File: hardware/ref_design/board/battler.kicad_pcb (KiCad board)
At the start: 2 copper layers, 73.4 x 127.7 mm, 177 parts, among them J1 TYPE-C-31-M-12, J2 53261-0271, J3 FH12-50S-0.5SH(55), J4 53261-0271, J5 SWD, J6 UART, J7 DEBUG PADS, Q1 2N7002, Q3 2N7002, Q5 AO3400A, Q6 AO3400A, Q7 2N7002, SW1 P1 UP, SW10 P2 DOWN, SW11 P2 LEFT, SW12 P2 RIGHT, SW13 P2 A, SW14 P2 B, SW15 P2 X, SW16 P2 Y, SW18 BOOTSEL, SW19 RESET, SW2 P1 DOWN, SW20 P1 SELECT, SW21 P1 START / PWR, SW22 P2 SELECT, SW23 P2 START / PWR, SW3 P1 LEFT, SW4 P1 RIGHT, SW5 P1 A, SW6 P1 B, SW7 P1 X, SW8 P1 Y, SW9 P2 UP, U1 SRV05-4, U2 BQ24073RGTR, U3 RT9013-33GB, U4 RP2354B, U6 MCP6002, U7 FM8002A, U8 SN74HC165PWR, U9 SN74HC165PWR, X1 12MHz

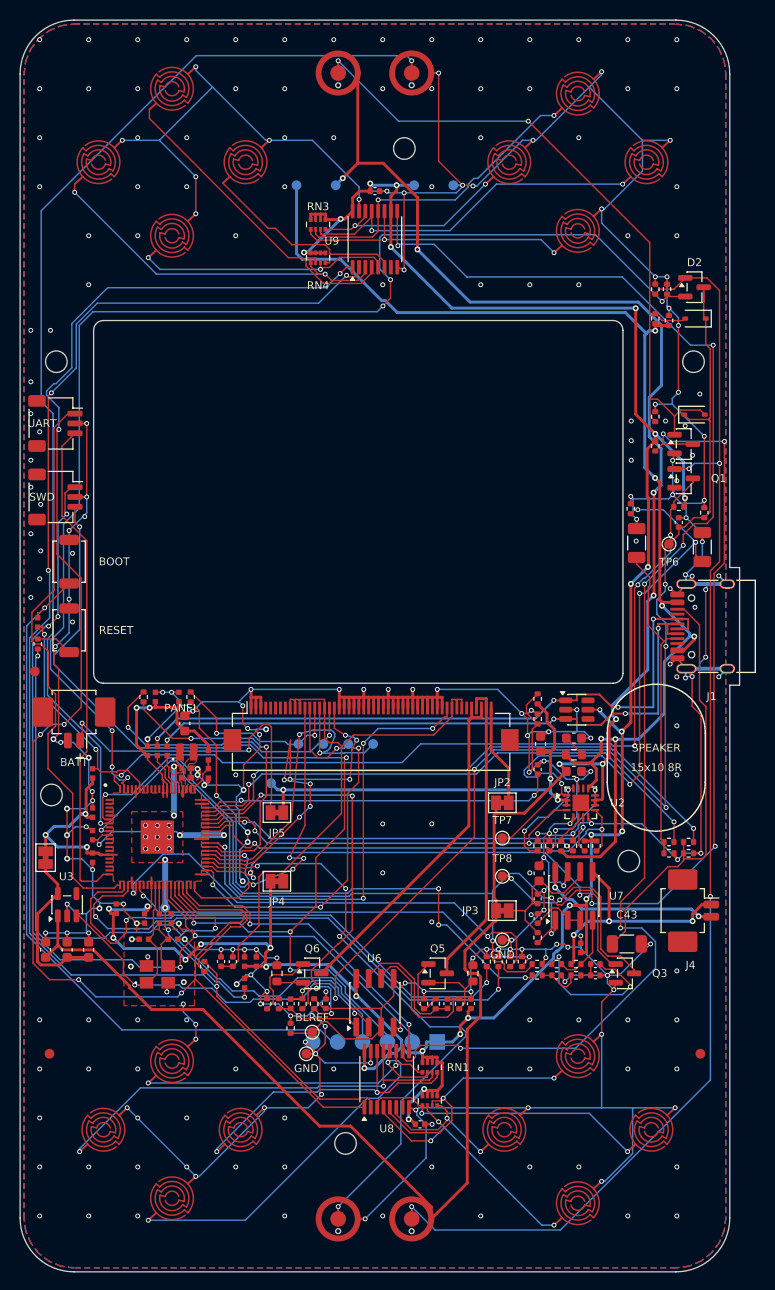
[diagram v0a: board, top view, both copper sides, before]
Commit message: ref_design levers: pins facing their nets, no REV straps, no UART, debug buttons and latch parts out of the strips
An experiment for Alex (not on ref-design-cellcut): make the board easier to route without
changing its size.
1. GPIOs: AUDIO_PWM 8 -> 31 (PWM7 B), AMP_EN 11 -> 34, BL_PWM 44 -> 28 (PWM6 A), PWR_HOLD
   2 -> 44, P2_START 34 -> 2, P2_SELECT 9 -> 4, SR_PL 28 -> 19 (datasheet Table 3 checked;
   U4's pin review updated)
2. REV0-REV3 and R48-R51 removed (the revision stays on the silkscreen)
3. J6 (UART) and C41 removed; SW18/SW19 out of the left strip into the left bezel below H4
   (U3 and its caps 2 mm down, JP1 below the core)
4. The latch's strip parts (Q1, R16, R15, C47, TP6, D8, Q7, R62, R63) up past the hole's
   top edge under seat 2's deck; C42 to the right bezel
tools/strip_load.py counts nets through each strip: 11/15 -> 8/11, parts 8/16 -> 3/5.
Routed clean on the first finished attempt (seed 3, 4.2 min); check_pcb and check_fit pass.

Co-Authored-By: Claude Opus 5.5 <noreply@anthropic.com>
Claude-Session: https://claude.ai/code/session_01Y3mFMxLYqNeyyedvbYuRwX
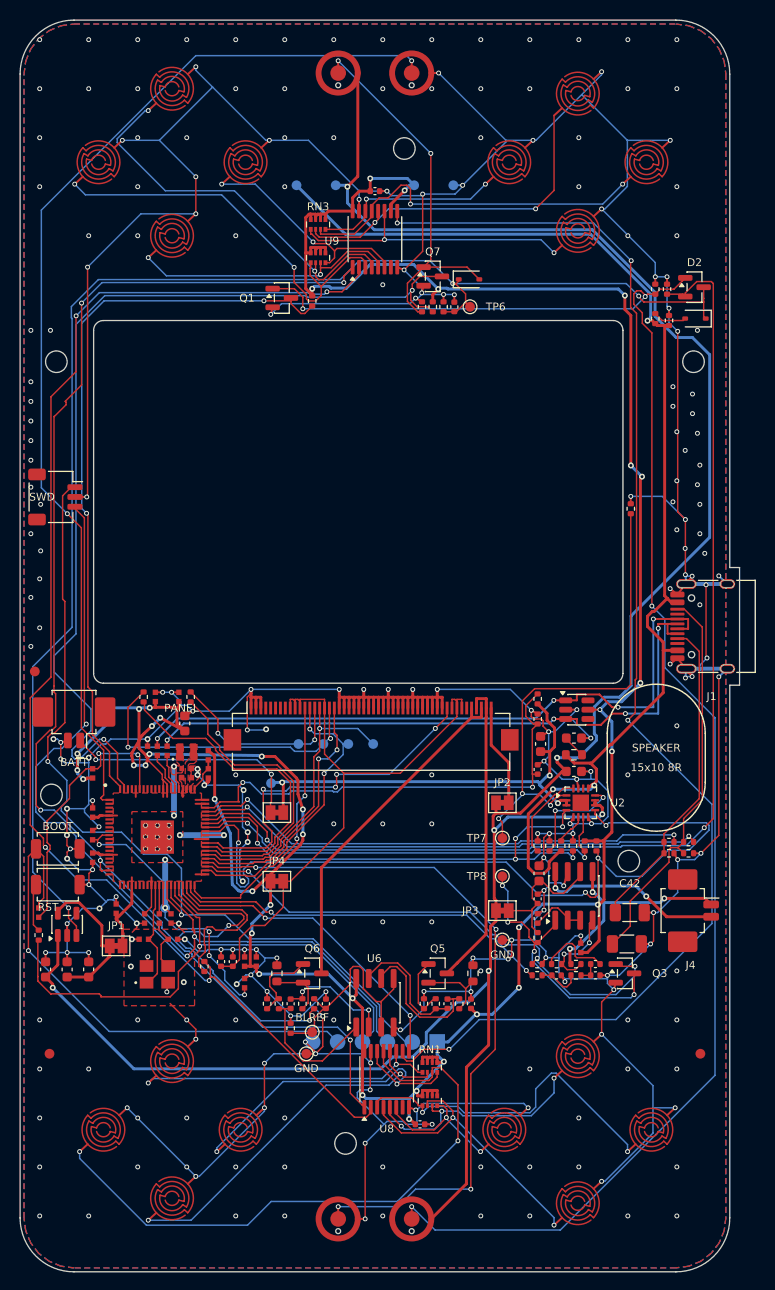
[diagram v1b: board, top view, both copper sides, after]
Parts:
- removed C41: DNP, Capacitor_SMD:C_1206_3216Metric
- removed J6: UART, battler:JST_SH_SM03B-SRSS-TB_1x03-1MP_P1.00mm_Horizontal
- removed R48: DNP, Resistor_SMD:R_0402_1005Metric
- removed R49, R50, R51: 1k, Resistor_SMD:R_0402_1005Metric
- moved Q1 44.9 mm to (90.5, 64.5)
- moved R16 42.9 mm to (93.6, 64.8), turned to 90 degrees
- moved C42 37.7 mm to (126.0, 127.2), turned to 0 degrees
- moved R15 33.9 mm to (107.0, 65.4)
- moved C47 31.8 mm to (108.1, 65.4)
- moved TP6 31.6 mm to (109.7, 65.4)
- moved Q7 30.8 mm to (105.9, 62.3)
- moved R26 29.7 mm to (65.7, 129.5)
- moved R25 29.6 mm to (65.7, 127.2)
- moved SW18 29.3 mm to (67.7, 120.7), turned to 0 degrees
- moved D8 26.8 mm to (109.6, 62.6)
- moved R63 26.8 mm to (105.9, 65.4)
- moved R62 26.3 mm to (104.8, 65.4)
- moved SW19 26.0 mm to (67.7, 124.3), turned to 0 degrees
- moved JP1 11.5 mm to (73.6, 130.6), turned to 0 degrees
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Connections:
- U4 pad 1: unconnected-(U4-GPIO4-Pad1) -> P2_SELECT
- U4 pad 19: unconnected-(U4-GPIO19-Pad19) -> SR_PL
- U4 pad 20: UART_TX -> unconnected-(U4-GPIO20-Pad20)
- U4 pad 21: UART_RX -> unconnected-(U4-GPIO21-Pad21)
- U4 pad 22: /MCU/REV0 -> unconnected-(U4-GPIO22-Pad22)
- U4 pad 23: /MCU/REV1 -> unconnected-(U4-GPIO23-Pad23)
- U4 pad 25: /MCU/REV2 -> unconnected-(U4-GPIO24-Pad25)
- U4 pad 26: /MCU/REV3 -> unconnected-(U4-GPIO25-Pad26)
- U4 pad 36: SR_PL -> BL_PWM
- U4 pad 39: unconnected-(U4-GPIO31-Pad39) -> AUDIO_PWM
- U4 pad 43: P2_START -> AMP_EN
- U4 pad 55: BL_PWM -> PWR_HOLD
- U4 pad 6: AUDIO_PWM -> unconnected-(U4-GPIO8-Pad6)
- U4 pad 7: P2_SELECT -> unconnected-(U4-GPIO9-Pad7)
- U4 pad 79: PWR_HOLD -> P2_START
- U4 pad 9: AMP_EN -> unconnected-(U4-GPIO11-Pad9)
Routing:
- net UART_RX: track 57.7 -> 0.00 mm
- net /MCU/REV0: track 55.6 -> 0.00 mm, vias 2 -> 0
- net /MCU/REV1: track 54.2 -> 0.00 mm, vias 2 -> 0
- net UART_TX: track 50.8 -> 0.00 mm
- net /MCU/REV2: track 49.8 -> 0.00 mm, vias 2 -> 0
- net /MCU/REV3: track 44.9 -> 0.00 mm, vias 2 -> 0
- net +3V3: track 309.3 -> 346.8 mm, vias 35 -> 37
- net PWR_BTN_RAW: track 132.6 -> 169.9 mm
- net CHG_STAT_N: track 48.5 -> 82.6 mm, vias 2 -> 4
- net AMP_EN: track 87.5 -> 55.0 mm
- net P2_START_RAW: track 67.9 -> 38.8 mm
- net RUN: track 83.2 -> 56.8 mm, vias 2 -> 1
- net SR_PL: track 160.9 -> 135.3 mm, vias 6 -> 5
- net AUDIO_PWM: track 64.4 -> 39.1 mm, vias 4 -> 2
- net /Debug/BOOTSEL: track 75.3 -> 52.7 mm
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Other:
- board text added: "RST"
- board text removed: "RESET"
- board text removed: "UART"

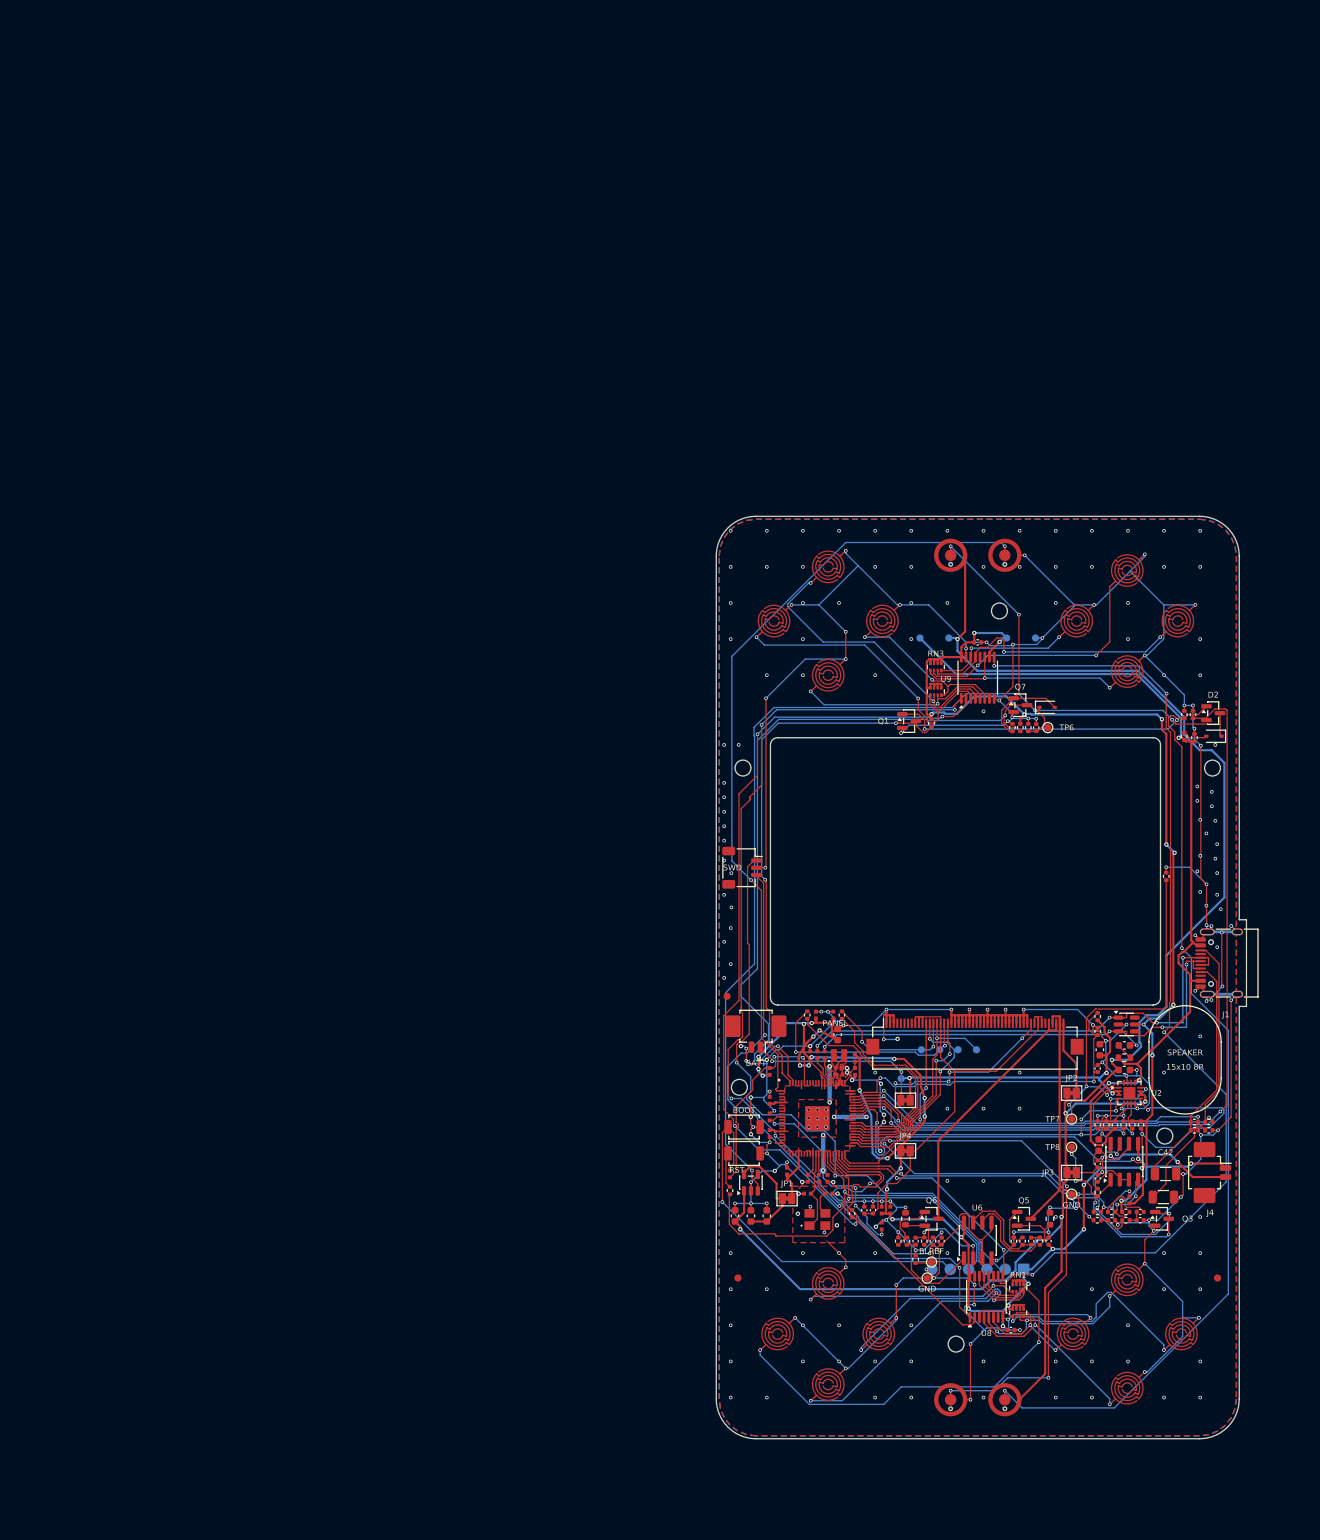
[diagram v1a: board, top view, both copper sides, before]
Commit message: ref_design: board routed for the 3.5 in panel (0 unconnected, DRC 0 errors); route.py's maze reaches across the board for SR_CHAIN
Co-Authored-By: Claude Sonnet 5.5 <noreply@anthropic.com>
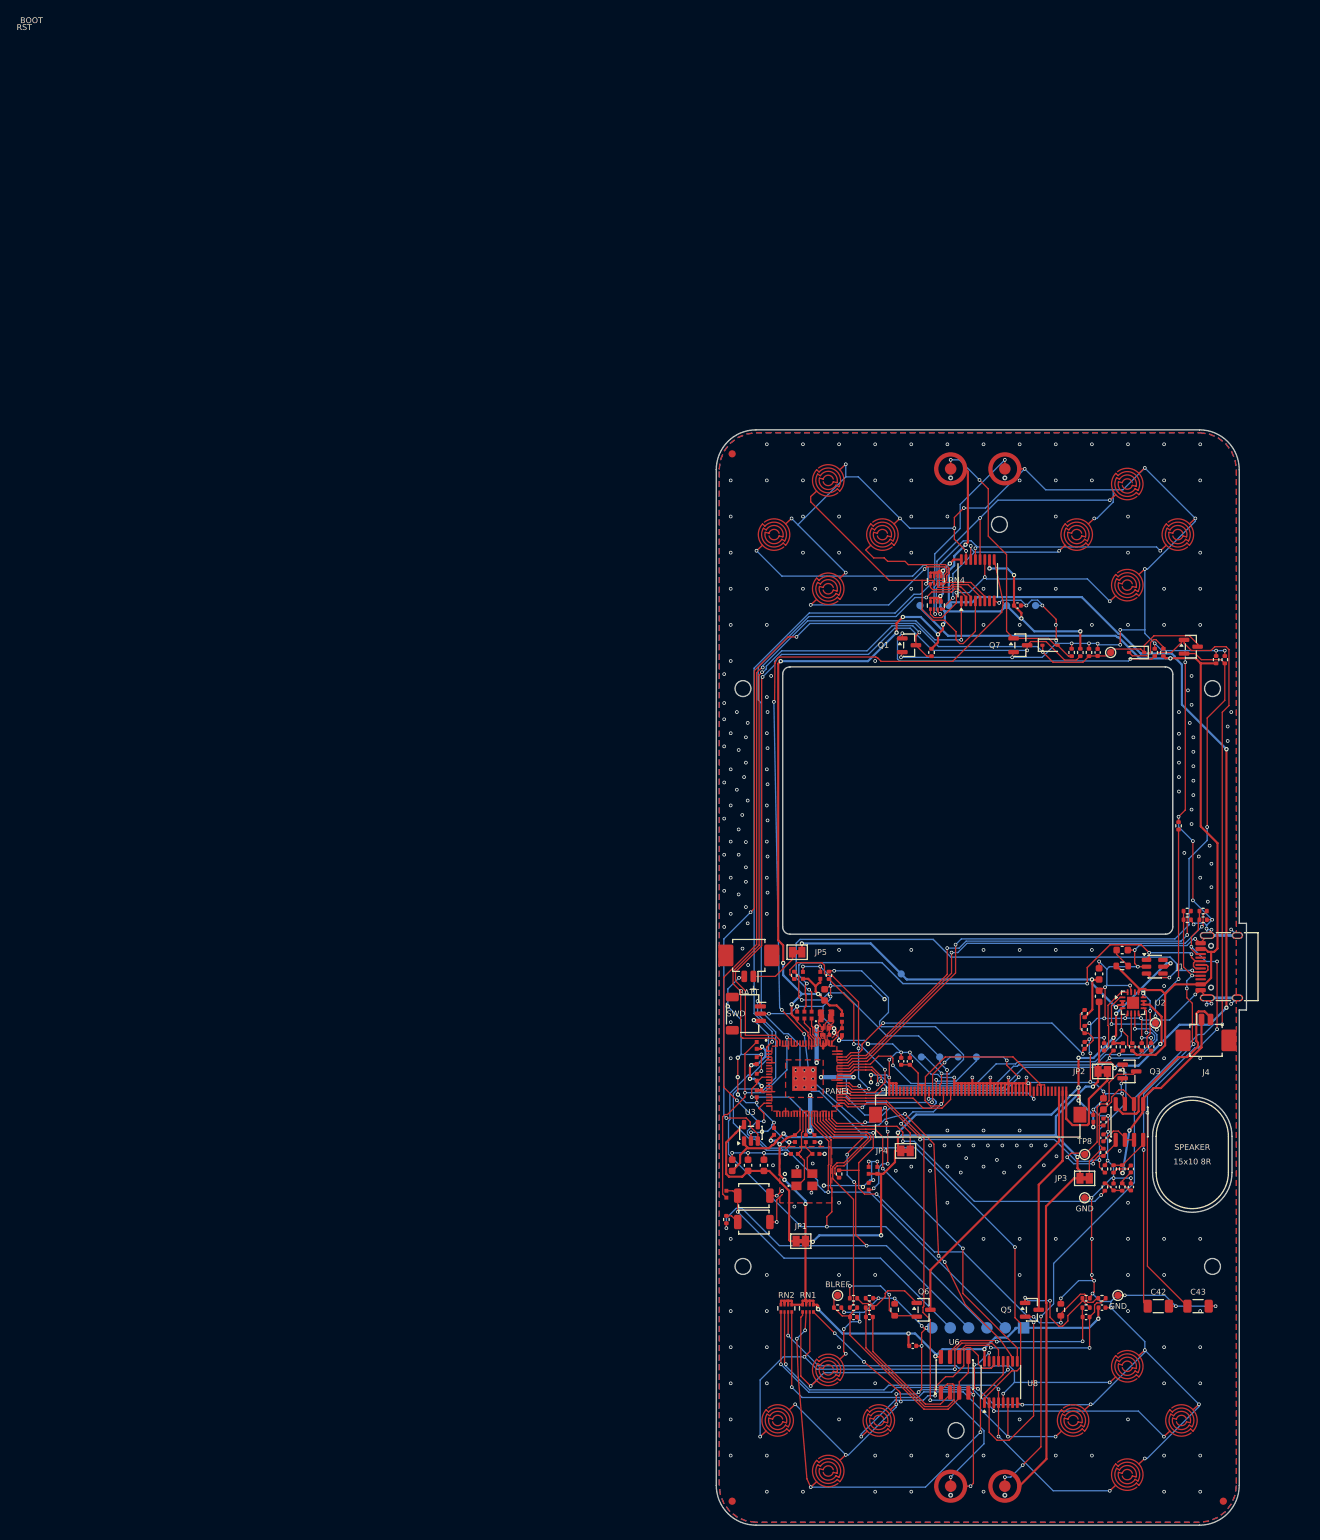
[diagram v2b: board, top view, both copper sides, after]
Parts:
- R61: value 2.4k -> 3.9k
- moved FID3 114.1 mm to (66.0, 27.5)
- moved FID1 69.9 mm to (66.0, 172.5)
- moved RN2 32.1 mm to (73.5, 145.8)
- moved FID2 30.9 mm to (134.0, 172.5)
- moved RN1 29.2 mm to (76.5, 145.8)
- moved R3 29.2 mm to (129.0, 90.8)
- moved R4 29.2 mm to (131.2, 90.8)
- moved R1 29.2 mm to (129.0, 92.0)
- moved R2 29.2 mm to (131.2, 92.0)
- moved TP16 26.5 mm to (119.4, 144.0)
- moved JP5 25.4 mm to (75.0, 96.5)
- moved H4 24.8 mm to (67.5, 140.0)
- moved C29 21.2 mm to (89.4, 111.6)
- moved C30 21.2 mm to (90.6, 111.6)
- moved Q3 20.9 mm to (121.0, 113.0)
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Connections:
- J3 pad 14: /Display/LCD_SCK -> LCD_DC
- J3 pad 15: LCD_DC -> /Display/LCD_SCK
- J3 pad 45: GND -> unconnected-(J3-Pin_45-Pad45)
- J3 pad 46: /Display/LED_K2 -> unconnected-(J3-Pin_46-Pad46)
- J3 pad 47: /Display/LED_K1 -> unconnected-(J3-Pin_47-Pad47)
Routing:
- net SR_PL: track 135.3 -> 178.8 mm
- net /Buttons/P1_Y: track 15.1 -> 56.2 mm, vias 2 -> 3
- net /Buttons/SR_CLK: track 136.0 -> 175.7 mm
- net /Buttons/P1_B: track 29.9 -> 65.0 mm, vias 2 -> 4
- net /Buttons/P1_A: track 35.5 -> 67.3 mm, vias 2 -> 3
- net /Buttons/P1_X: track 24.8 -> 56.2 mm
- net /USB_Charger/CC1: track 33.0 -> 60.2 mm, vias 0 -> 4
- net CHG_STAT_N: track 82.6 -> 55.4 mm, vias 4 -> 3
- net /USB_Charger/CC2: track 40.7 -> 66.0 mm, vias 0 -> 4
- net /Buttons/P1_DOWN: track 39.3 -> 63.8 mm, vias 2 -> 4
- net VSYS: track 239.2 -> 260.5 mm, vias 6 -> 8
- net /Buttons/SR_CHAIN: track 136.6 -> 157.0 mm, vias 4 -> 6
- net /Display/LCD_SCK: track 19.1 -> 38.3 mm
- net /USB_Charger/CELL_P: track 25.1 -> 7.38 mm, vias 2 -> 0
- net SR_DATA: track 32.5 -> 48.4 mm
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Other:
- board size 73.4 x 127.7 mm -> 73.4 x 151.6 mm
